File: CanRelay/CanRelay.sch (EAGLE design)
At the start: 20 parts

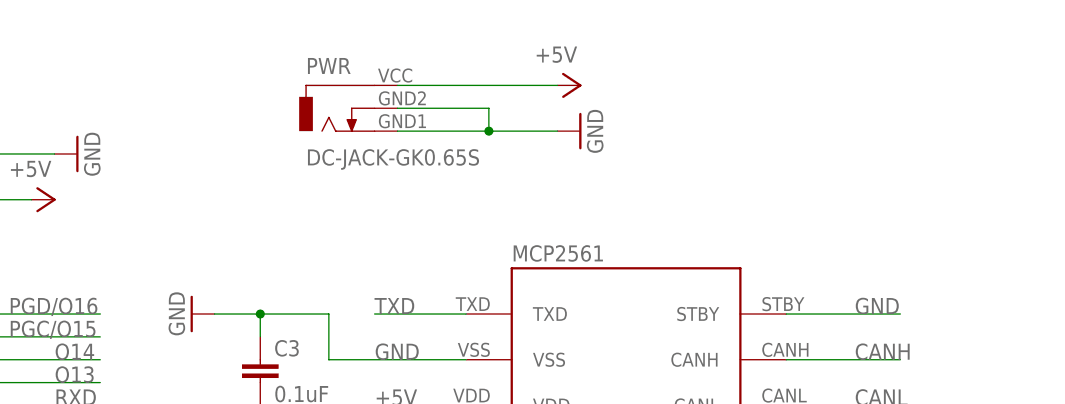
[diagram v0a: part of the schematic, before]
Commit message: #12 dropping 2 new power jacks into the schematic and connecting. Only dropping into the board, not yet aligning up all
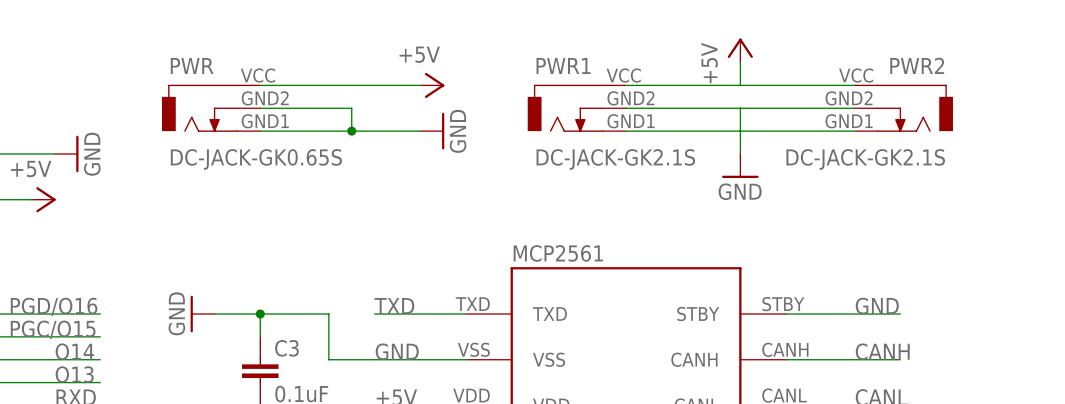
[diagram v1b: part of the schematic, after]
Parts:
- added PWR1, PWR2: DC-JACK-GK2.1S, PoJD:DC-JACK-GK2.1S
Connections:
- net +5V: now also PWR1.VCC, PWR2.VCC
- net GND: now also PWR1.GND1, PWR1.GND2, PWR2.GND1, PWR2.GND2
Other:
- moved on the sheet: PWR
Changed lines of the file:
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@@
 <?xml version="1.0" encoding="utf-8"?>
 <!DOCTYPE eagle SYSTEM "eagle.dtd">
-<eagle version="7.6.0">
+<eagle version="7.7.0">
 <drawing>
 <settings>
@@
 <grid distance="0.1" unitdist="inch" unit="inch" style="lines" multiple="1" display="no" altdistance="0.01" altunitdist="inch" altunit="inch"/>
 <layers>
-<layer number="1" name="Top" color="4" fill="1" visible="yes" active="no"/>
-<layer number="16" name="Bottom" color="1" fill="1" visible="yes" active="no"/>
-<layer number="17" name="Pads" color="2" fill="1" visible="yes" active="no"/>
-<layer number="18" name="Vias" color="2" fill="1" visible="yes" active="no"/>
-<layer number="19" name="Unrouted" color="6" fill="1" visible="yes" active="no"/>
-<layer number="20" name="Dimension" color="15" fill="1" visible="yes" active="no"/>
-<layer number="21" name="tPlace" color="7" fill="1" visible="yes" active="no"/>
-<layer number="22" name="bPlace" color="7" fill="1" visible="yes" active="no"/>
-<layer number="23" name="tOrigins" color="15" fill="1" visible="yes" active="no"/>
-<layer number="24" name="bOrigins" color="15" fill="1" visible="yes" active="no"/>
-<layer number="25" name="tNames" color="7" fill="1" visible="yes" active="no"/>
-<layer number="26" name="bNames" color="7" fill="1" visible="yes" active="no"/>
-<layer number="27" name="tValues" color="7" fill="1" visible="yes" active="no"/>
-<layer number="28" name="bValues" color="7" fill="1" visible="yes" active="no"/>
+<layer number="1" name="Top" color="4" fill="1" visible="no" active="no"/>
+<layer number="16" name="Bottom" color="1" fill="1" visible="no" active="no"/>
+<layer number="17" name="Pads" color="2" fill="1" visible="no" active="no"/>
+<layer number="18" name="Vias" color="2" fill="1" visible="no" active="no"/>
+<layer number="19" name="Unrouted" color="6" fill="1" visible="no" active="no"/>
+<layer number="20" name="Dimension" color="15" fill="1" visible="no" active="no"/>
+<layer number="21" name="tPlace" color="7" fill="1" visible="no" active="no"/>
+<layer number="22" name="bPlace" color="7" fill="1" visible="no" active="no"/>
+<layer number="23" name="tOrigins" color="15" fill="1" visible="no" active="no"/>
+<layer number="24" name="bOrigins" color="15" fill="1" visible="no" active="no"/>
+<layer number="25" name="tNames" color="7" fill="1" visible="no" active="no"/>
+<layer number="26" name="bNames" color="7" fill="1" visible="no" active="no"/>
+<layer number="27" name="tValues" color="7" fill="1" visible="no" active="no"/>
+<layer number="28" name="bValues" color="7" fill="1" visible="no" active="no"/>
 <layer number="29" name="tStop" color="7" fill="3" visible="no" active="no"/>
 <layer number="30" name="bStop" color="7" fill="6" visible="no" active="no"/>
@@
 <layer number="35" name="tGlue" color="7" fill="4" visible="no" active="no"/>
 <layer number="36" name="bGlue" color="7" fill="5" visible="no" active="no"/>
-<layer number="37" name="tTest" color="7" fill="1" visible="yes" active="no"/>
-<layer number="38" name="bTest" color="7" fill="1" visible="yes" active="no"/>
+<layer number="37" name="tTest" color="7" fill="1" visible="no" active="no"/>
+<layer number="38" name="bTest" color="7" fill="1" visible="no" active="no"/>
 <layer number="39" name="tKeepout" color="4" fill="11" visible="no" active="no"/>
 <layer number="40" name="bKeepout" color="1" fill="11" visible="no" active="no"/>
@@
 <layer number="44" name="Drills" color="7" fill="1" visible="no" active="no"/>
 <layer number="45" name="Holes" color="7" fill="1" visible="no" active="no"/>
-<layer number="46" name="Milling" color="3" fill="1" visible="yes" active="no"/>
-<layer number="47" name="Measures" color="7" fill="1" visible="yes" active="no"/>
-<layer number="48" name="Document" color="7" fill="1" visible="yes" active="no"/>
-<layer number="49" name="Reference" color="7" fill="1" visible="yes" active="no"/>
-<layer number="51" name="tDocu" color="7" fill="1" visible="yes" active="no"/>
-<layer number="52" name="bDocu" color="7" fill="1" visible="yes" active="no"/>
+<layer number="46" name="Milling" color="3" fill="1" visible="no" active="no"/>
+<layer number="47" name="Measures" color="7" fill="1" visible="no" active="no"/>
+<layer number="48" name="Document" color="7" fill="1" visible="no" active="no"/>
+<layer number="49" name="Reference" color="7" fill="1" visible="no" active="no"/>
+<layer number="51" name="tDocu" color="7" fill="1" visible="no" active="no"/>
+<layer number="52" name="bDocu" color="7" fill="1" visible="no" active="no"/>
 <layer number="90" name="Modules" color="5" fill="1" visible="yes" active="yes"/>
 <layer number="91" name="Nets" color="2" fill="1" visible="yes" active="yes"/>
@@
 <part name="P+5" library="supply1" deviceset="+5V" device=""/>
 <part name="USBTIN" library="pinhead" deviceset="PINHD-1X3" device=""/>
+<part name="PWR1" library="PoJD" deviceset="DC-JACK-GK2.1" device="S"/>
+<part name="PWR2" library="PoJD" deviceset="DC-JACK-GK2.1" device="S"/>
+<part name="P+6" library="supply1" deviceset="+5V" device=""/>
+<part name="GND10" library="supply1" deviceset="GND" device=""/>
 </parts>
 <sheets>
@@
 <instance part="GND7" gate="1" x="-40.64" y="121.92" rot="R90"/>
 <instance part="GND8" gate="1" x="-106.68" y="121.92" rot="R270"/>
-<instance part="PWR" gate="G$1" x="-12.7" y="127"/>
-<instance part="GND9" gate="1" x="15.24" y="124.46" rot="R90"/>
-<instance part="P+5" gate="1" x="15.24" y="129.54" rot="R270"/>
+<instance part="PWR" gate="G$1" x="-27.94" y="127"/>
+<instance part="GND9" gate="1" x="0" y="124.46" rot="R90"/>
+<instance part="P+5" gate="1" x="0" y="129.54" rot="R270"/>
 <instance part="USBTIN" gate="A" x="7.62" y="50.8"/>
+<instance part="PWR1" gate="G$1" x="12.7" y="127"/>
+<instance part="PWR2" gate="G$1" x="53.34" y="127" rot="MR0"/>
+<instance part="P+6" gate="1" x="33.02" y="134.62"/>
+<instance part="GND10" gate="1" x="33.02" y="119.38"/>
 </instances>
 <busses>
@@
 <pinref part="PWR" gate="G$1" pin="VCC"/>
 <pinref part="P+5" gate="1" pin="+5V"/>
-<wire x1="-5.08" y1="129.54" x2="12.7" y2="129.54" width="0.1524" layer="91"/>
+<wire x1="-20.32" y1="129.54" x2="-2.54" y2="129.54" width="0.1524" layer="91"/>
+</segment>
+<segment>
+<pinref part="PWR1" gate="G$1" pin="VCC"/>
+<pinref part="PWR2" gate="G$1" pin="VCC"/>
+<wire x1="20.32" y1="129.54" x2="33.02" y2="129.54" width="0.1524" layer="91"/>
+<wire x1="33.02" y1="129.54" x2="45.72" y2="129.54" width="0.1524" layer="91"/>
+<wire x1="33.02" y1="129.54" x2="33.02" y2="132.08" width="0.1524" layer="91"/>
+<pinref part="P+6" gate="1" pin="+5V"/>
 </segment>
 </net>
@@
 <pinref part="PWR" gate="G$1" pin="GND1"/>
 <pinref part="GND9" gate="1" pin="GND"/>
-<wire x1="-5.08" y1="124.46" x2="5.08" y2="124.46" width="0.1524" layer="91"/>
+<wire x1="-20.32" y1="124.46" x2="-10.16" y2="124.46" width="0.1524" layer="91"/>
 <pinref part="PWR" gate="G$1" pin="GND2"/>
-<wire x1="5.08" y1="124.46" x2="12.7" y2="124.46" width="0.1524" layer="91"/>
-<wire x1="-5.08" y1="127" x2="5.08" y2="127" width="0.1524" layer="91"/>
-<wire x1="5.08" y1="127" x2="5.08" y2="124.46" width="0.1524" layer="91"/>
-<junction x="5.08" y="124.46"/>
+<wire x1="-10.16" y1="124.46" x2="-2.54" y2="124.46" width="0.1524" layer="91"/>
+<wire x1="-20.32" y1="127" x2="-10.16" y2="127" width="0.1524" layer="91"/>
+<wire x1="-10.16" y1="127" x2="-10.16" y2="124.46" width="0.1524" layer="91"/>
+<junction x="-10.16" y="124.46"/>
 </segment>
 <segment>
@@
 <label x="-7.62" y="48.26" size="1.778" layer="95"/>
 </segment>
+<segment>
+<pinref part="PWR2" gate="G$1" pin="GND1"/>
+<pinref part="PWR1" gate="G$1" pin="GND1"/>
+<wire x1="45.72" y1="124.46" x2="33.02" y2="124.46" width="0.1524" layer="91"/>
+<pinref part="PWR1" gate="G$1" pin="GND2"/>
+<pinref part="PWR2" gate="G$1" pin="GND2"/>
+<wire x1="33.02" y1="124.46" x2="20.32" y2="124.46" width="0.1524" layer="91"/>
+<wire x1="20.32" y1="127" x2="33.02" y2="127" width="0.1524" layer="91"/>
+<wire x1="33.02" y1="127" x2="45.72" y2="127" width="0.1524" layer="91"/>
+<wire x1="33.02" y1="127" x2="33.02" y2="124.46" width="0.1524" layer="91"/>
+<wire x1="33.02" y1="124.46" x2="33.02" y2="121.92" width="0.1524" layer="91"/>
+<pinref part="GND10" gate="1" pin="GND"/>
+</segment>
 </net>

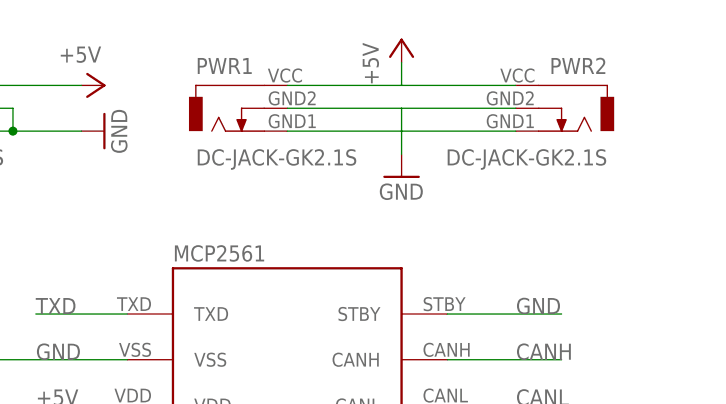
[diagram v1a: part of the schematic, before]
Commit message: #12 dropping the 2 and replacing with jut 1 new power jack, aliging all in board, not yet wiring all up since will need one more change to mirror the RJ45 connector anyway. but space now sufficient for new power jack
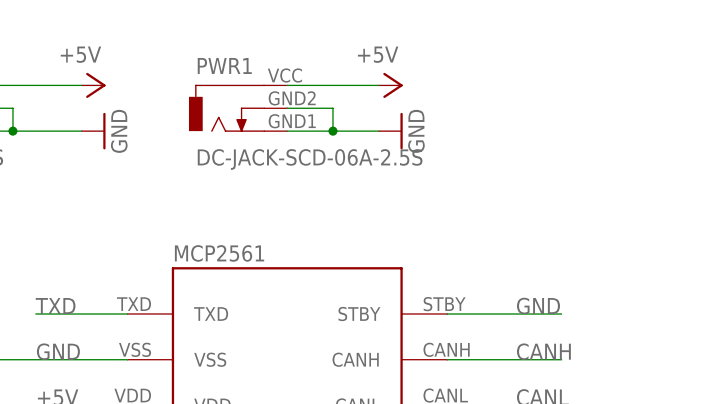
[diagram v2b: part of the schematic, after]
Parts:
- removed PWR2: DC-JACK-GK2.1S, PoJD:DC-JACK-GK2.1S
- PWR1: value DC-JACK-GK2.1S -> DC-JACK-SCD-06A-2.5S; device PoJD:DC-JACK-GK2.1S -> PoJD:DC-JACK-SCD-06A-2.5S
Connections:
- net +5V: no longer PWR2.VCC
- net GND: no longer PWR2.GND1, PWR2.GND2
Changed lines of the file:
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@@
 <part name="P+5" library="supply1" deviceset="+5V" device=""/>
 <part name="USBTIN" library="pinhead" deviceset="PINHD-1X3" device=""/>
-<part name="PWR1" library="PoJD" deviceset="DC-JACK-GK2.1" device="S"/>
-<part name="PWR2" library="PoJD" deviceset="DC-JACK-GK2.1" device="S"/>
 <part name="P+6" library="supply1" deviceset="+5V" device=""/>
 <part name="GND10" library="supply1" deviceset="GND" device=""/>
+<part name="PWR1" library="PoJD" deviceset="DC-JACK-SCD-06A-2.5" device="S"/>
 </parts>
 <sheets>
@@
 <instance part="P+5" gate="1" x="0" y="129.54" rot="R270"/>
 <instance part="USBTIN" gate="A" x="7.62" y="50.8"/>
+<instance part="P+6" gate="1" x="33.02" y="129.54" rot="R270"/>
+<instance part="GND10" gate="1" x="33.02" y="124.46" rot="R90"/>
 <instance part="PWR1" gate="G$1" x="12.7" y="127"/>
-<instance part="PWR2" gate="G$1" x="53.34" y="127" rot="MR0"/>
-<instance part="P+6" gate="1" x="33.02" y="134.62"/>
-<instance part="GND10" gate="1" x="33.02" y="119.38"/>
 </instances>
 <busses>
@@
 <segment>
 <pinref part="PWR1" gate="G$1" pin="VCC"/>
-<pinref part="PWR2" gate="G$1" pin="VCC"/>
-<wire x1="20.32" y1="129.54" x2="33.02" y2="129.54" width="0.1524" layer="91"/>
-<wire x1="33.02" y1="129.54" x2="45.72" y2="129.54" width="0.1524" layer="91"/>
-<wire x1="33.02" y1="129.54" x2="33.02" y2="132.08" width="0.1524" layer="91"/>
 <pinref part="P+6" gate="1" pin="+5V"/>
+<wire x1="20.32" y1="129.54" x2="30.48" y2="129.54" width="0.1524" layer="91"/>
 </segment>
 </net>
@@
 </segment>
 <segment>
-<pinref part="PWR2" gate="G$1" pin="GND1"/>
+<pinref part="PWR1" gate="G$1" pin="GND2"/>
+<wire x1="20.32" y1="127" x2="25.4" y2="127" width="0.1524" layer="91"/>
+<wire x1="25.4" y1="127" x2="25.4" y2="124.46" width="0.1524" layer="91"/>
 <pinref part="PWR1" gate="G$1" pin="GND1"/>
-<wire x1="45.72" y1="124.46" x2="33.02" y2="124.46" width="0.1524" layer="91"/>
-<pinref part="PWR1" gate="G$1" pin="GND2"/>
-<pinref part="PWR2" gate="G$1" pin="GND2"/>
-<wire x1="33.02" y1="124.46" x2="20.32" y2="124.46" width="0.1524" layer="91"/>
-<wire x1="20.32" y1="127" x2="33.02" y2="127" width="0.1524" layer="91"/>
-<wire x1="33.02" y1="127" x2="45.72" y2="127" width="0.1524" layer="91"/>
-<wire x1="33.02" y1="127" x2="33.02" y2="124.46" width="0.1524" layer="91"/>
-<wire x1="33.02" y1="124.46" x2="33.02" y2="121.92" width="0.1524" layer="91"/>
+<wire x1="20.32" y1="124.46" x2="25.4" y2="124.46" width="0.1524" layer="91"/>
 <pinref part="GND10" gate="1" pin="GND"/>
+<wire x1="25.4" y1="124.46" x2="30.48" y2="124.46" width="0.1524" layer="91"/>
+<junction x="25.4" y="124.46"/>
 </segment>
 </net>

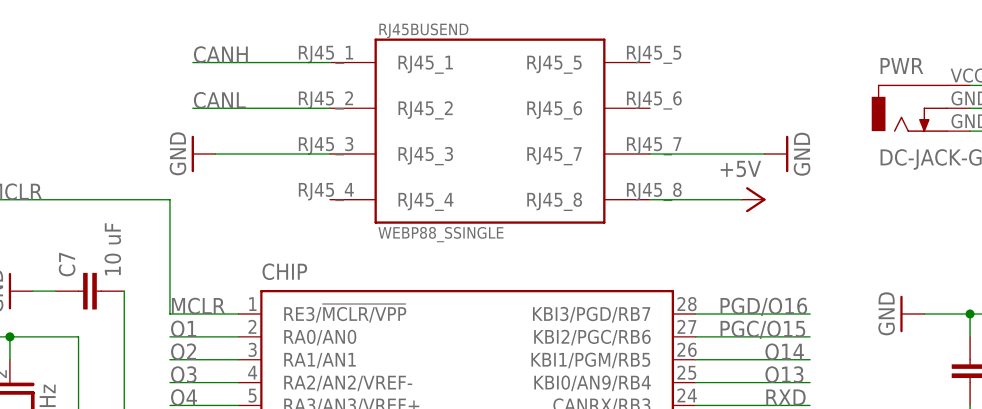
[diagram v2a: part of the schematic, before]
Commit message: #10 mirroring pins on RJ45 and wiring up remainder to +5V and GND in schematic. Started work in board - rewired all +5V in thicker wire everywhere. wired up RJ45 +5V and GND pins, CAN lines and RX and TX lines between transceiver and chip unwire now still
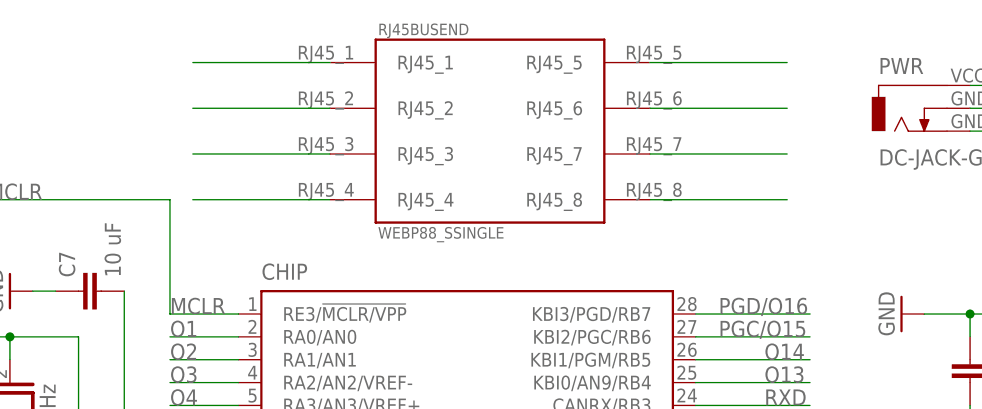
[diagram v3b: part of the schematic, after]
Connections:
- net +5V: now also RJ45BUSEND.RJ45_1, RJ45BUSEND.RJ45_3, RJ45BUSEND.RJ45_5; no longer RJ45BUSEND.RJ45_8
- net CANH: now also RJ45BUSEND.RJ45_8; no longer RJ45BUSEND.RJ45_1
- net CANL: now also RJ45BUSEND.RJ45_7; no longer RJ45BUSEND.RJ45_2
- net GND: now also RJ45BUSEND.RJ45_2, RJ45BUSEND.RJ45_4, RJ45BUSEND.RJ45_6; no longer RJ45BUSEND.RJ45_3, RJ45BUSEND.RJ45_7
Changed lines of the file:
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@@
 <part name="OUTPUTS" library="pinhead" deviceset="PINHD-2X10" device=""/>
 <part name="RJ45BUSEND" library="PoJD" deviceset="WEBP88_S" device="SINGLE"/>
-<part name="P+4" library="supply1" deviceset="+5V" device=""/>
-<part name="GND7" library="supply1" deviceset="GND" device=""/>
-<part name="GND8" library="supply1" deviceset="GND" device=""/>
 <part name="PWR" library="PoJD" deviceset="DC-JACK-GK0.65" device="S"/>
 <part name="GND9" library="supply1" deviceset="GND" device=""/>
@@
 <instance part="OUTPUTS" gate="A" x="-93.98" y="45.72"/>
 <instance part="RJ45BUSEND" gate="G$1" x="-73.66" y="124.46"/>
-<instance part="P+4" gate="1" x="-43.18" y="116.84" rot="R270"/>
-<instance part="GND7" gate="1" x="-40.64" y="121.92" rot="R90"/>
-<instance part="GND8" gate="1" x="-106.68" y="121.92" rot="R270"/>
 <instance part="PWR" gate="G$1" x="-27.94" y="127"/>
 <instance part="GND9" gate="1" x="0" y="124.46" rot="R90"/>
@@
 </segment>
 <segment>
-<pinref part="RJ45BUSEND" gate="G$1" pin="RJ45_8"/>
-<pinref part="P+4" gate="1" pin="+5V"/>
-<wire x1="-55.88" y1="116.84" x2="-45.72" y2="116.84" width="0.1524" layer="91"/>
-</segment>
-<segment>
 <pinref part="PWR" gate="G$1" pin="VCC"/>
 <pinref part="P+5" gate="1" pin="+5V"/>
@@
 <pinref part="P+6" gate="1" pin="+5V"/>
 <wire x1="20.32" y1="129.54" x2="30.48" y2="129.54" width="0.1524" layer="91"/>
+</segment>
+<segment>
+<pinref part="RJ45BUSEND" gate="G$1" pin="RJ45_1"/>
+<wire x1="-91.44" y1="132.08" x2="-106.68" y2="132.08" width="0.1524" layer="91"/>
+</segment>
+<segment>
+<pinref part="RJ45BUSEND" gate="G$1" pin="RJ45_3"/>
+<wire x1="-91.44" y1="121.92" x2="-106.68" y2="121.92" width="0.1524" layer="91"/>
+</segment>
+<segment>
+<pinref part="RJ45BUSEND" gate="G$1" pin="RJ45_5"/>
+<wire x1="-55.88" y1="132.08" x2="-40.64" y2="132.08" width="0.1524" layer="91"/>
 </segment>
 </net>
@@
 </segment>
 <segment>
-<pinref part="RJ45BUSEND" gate="G$1" pin="RJ45_7"/>
-<pinref part="GND7" gate="1" pin="GND"/>
-<wire x1="-55.88" y1="121.92" x2="-43.18" y2="121.92" width="0.1524" layer="91"/>
-</segment>
-<segment>
-<pinref part="RJ45BUSEND" gate="G$1" pin="RJ45_3"/>
-<pinref part="GND8" gate="1" pin="GND"/>
-<wire x1="-91.44" y1="121.92" x2="-104.14" y2="121.92" width="0.1524" layer="91"/>
-</segment>
-<segment>
 <pinref part="PWR" gate="G$1" pin="GND1"/>
 <pinref part="GND9" gate="1" pin="GND"/>
@@
 <wire x1="25.4" y1="124.46" x2="30.48" y2="124.46" width="0.1524" layer="91"/>
 <junction x="25.4" y="124.46"/>
+</segment>
+<segment>
+<pinref part="RJ45BUSEND" gate="G$1" pin="RJ45_2"/>
+<wire x1="-91.44" y1="127" x2="-106.68" y2="127" width="0.1524" layer="91"/>
+</segment>
+<segment>
+<pinref part="RJ45BUSEND" gate="G$1" pin="RJ45_4"/>
+<wire x1="-91.44" y1="116.84" x2="-106.68" y2="116.84" width="0.1524" layer="91"/>
+</segment>
+<segment>
+<pinref part="RJ45BUSEND" gate="G$1" pin="RJ45_6"/>
+<wire x1="-55.88" y1="127" x2="-40.64" y2="127" width="0.1524" layer="91"/>
 </segment>
 </net>
@@
 </segment>
 <segment>
-<pinref part="RJ45BUSEND" gate="G$1" pin="RJ45_1"/>
-<wire x1="-91.44" y1="132.08" x2="-106.68" y2="132.08" width="0.1524" layer="91"/>
-<label x="-106.68" y="132.08" size="1.778" layer="95"/>
-</segment>
-<segment>
 <pinref part="USBTIN" gate="A" pin="1"/>
 <wire x1="5.08" y1="53.34" x2="-7.62" y2="53.34" width="0.1524" layer="91"/>
 <label x="-7.62" y="53.34" size="1.778" layer="95"/>
 </segment>
+<segment>
+<pinref part="RJ45BUSEND" gate="G$1" pin="RJ45_8"/>
+<wire x1="-55.88" y1="116.84" x2="-40.64" y2="116.84" width="0.1524" layer="91"/>
+</segment>
 </net>
 <net name="CANL" class="0">
@@
 </segment>
 <segment>
-<pinref part="RJ45BUSEND" gate="G$1" pin="RJ45_2"/>
-<wire x1="-91.44" y1="127" x2="-106.68" y2="127" width="0.1524" layer="91"/>
-<label x="-106.68" y="127" size="1.778" layer="95"/>
-</segment>
-<segment>
 <pinref part="USBTIN" gate="A" pin="2"/>
 <wire x1="5.08" y1="50.8" x2="-7.62" y2="50.8" width="0.1524" layer="91"/>
 <label x="-7.62" y="50.8" size="1.778" layer="95"/>
 </segment>
-</net>
+<segment>
+<pinref part="RJ45BUSEND" gate="G$1" pin="RJ45_7"/>
+<wire x1="-55.88" y1="121.92" x2="-40.64" y2="121.92" width="0.1524" layer="91"/>
+</segment>
+</net>
